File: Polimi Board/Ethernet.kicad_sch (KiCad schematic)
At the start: 17 parts, among them J6 RJ45_Wuerth_7499010121A, U3 LAN8742A

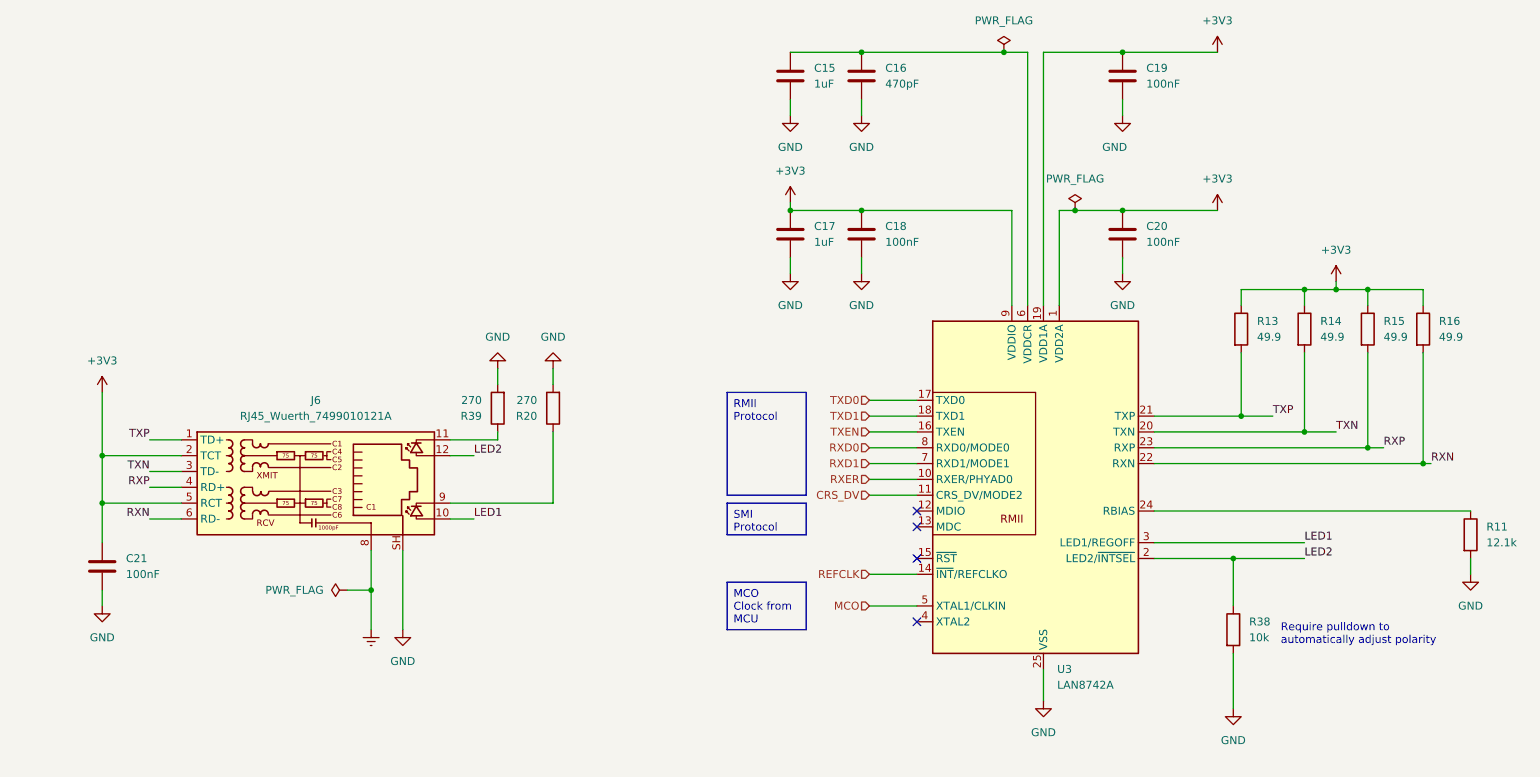
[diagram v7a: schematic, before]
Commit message: adjusted some violations of ERC test
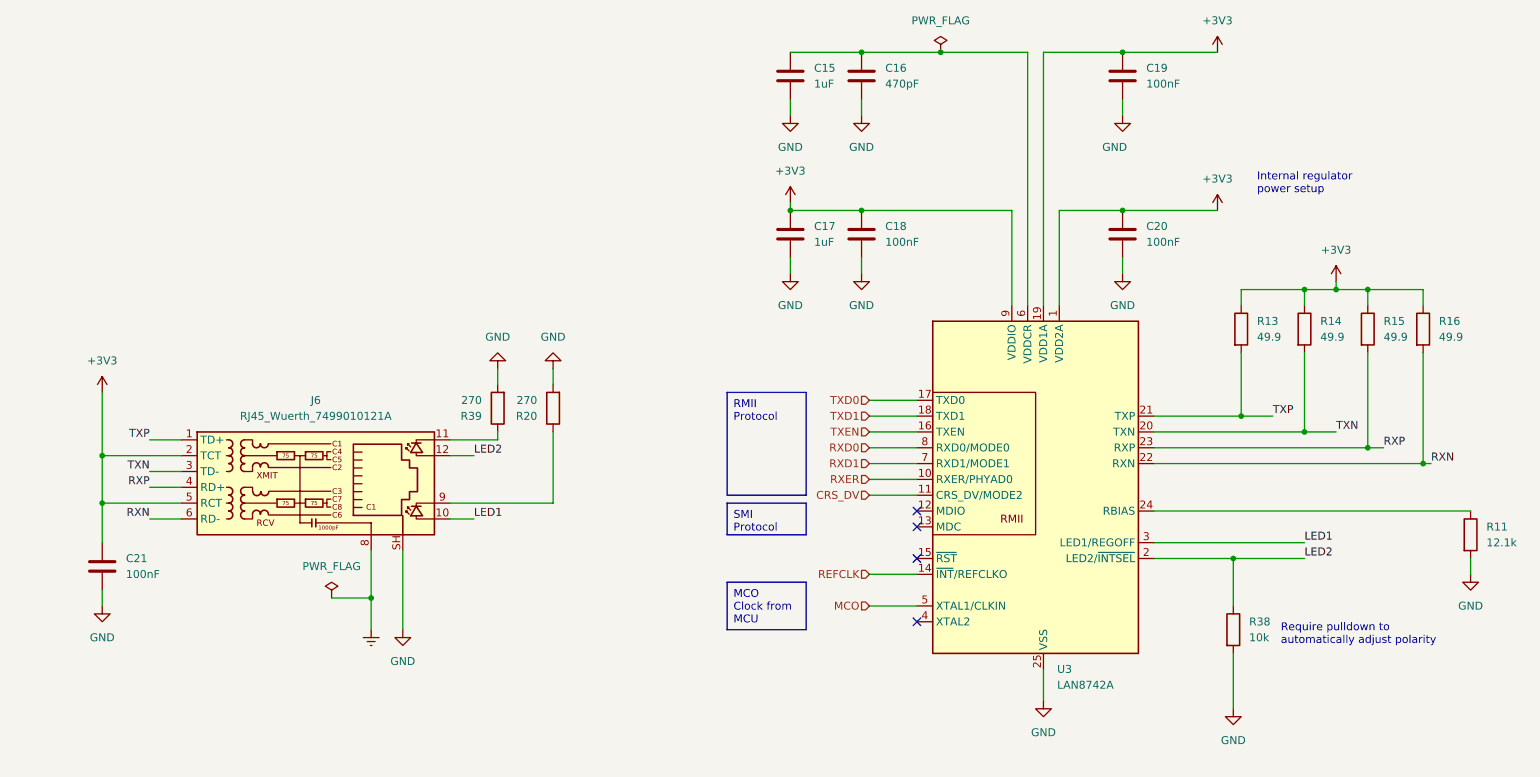
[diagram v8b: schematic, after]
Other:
- note added: "Internal regulator power setup"
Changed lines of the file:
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@@
     (comment 2 "ing. Zaccaria Eliseo Carrettoni")
   )
-  (junction (at 182.88 34.29) (diameter 0) (color 0 0 0 0)
-  )
   (junction (at 236.22 72.39) (diameter 0) (color 0 0 0 0)
   )
@@
   (junction (at 148.59 59.69) (diameter 0) (color 0 0 0 0)
   )
-  (junction (at 194.31 59.69) (diameter 0) (color 0 0 0 0)
-  )
-  (junction (at 81.28 120.65) (diameter 0) (color 0 0 0 0)
-  )
   (junction (at 38.1 106.68) (diameter 0) (color 0 0 0 0)
   )
@@
   (junction (at 160.02 34.29) (diameter 0) (color 0 0 0 0)
   )
+  (junction (at 81.28 121.92) (diameter 0) (color 0 0 0 0)
+  )
   (junction (at 241.3 97.79) (diameter 0) (color 0 0 0 0)
   )
@@
   )
   (junction (at 241.3 72.39) (diameter 0) (color 0 0 0 0)
+  )
+  (junction (at 172.72 34.29) (diameter 0) (color 0 0 0 0)
   )
   (junction (at 160.02 59.69) (diameter 0) (color 0 0 0 0)
@@
     (stroke (width 0) (type default))
   )
-  (wire (pts (xy 160.02 34.29) (xy 182.88 34.29))
-    (stroke (width 0) (type default))
-  )
   (wire (pts (xy 148.59 41.91) (xy 148.59 44.45))
     (stroke (width 0) (type default))
@@
     (stroke (width 0) (type default))
   )
+  (wire (pts (xy 74.93 121.92) (xy 81.28 121.92))
+    (stroke (width 0) (type default))
+  )
   (wire (pts (xy 219.71 130.81) (xy 219.71 139.7))
     (stroke (width 0) (type default))
@@
     (stroke (width 0) (type default))
   )
+  (wire (pts (xy 81.28 121.92) (xy 81.28 127))
+    (stroke (width 0) (type default))
+  )
+  (wire (pts (xy 81.28 114.3) (xy 81.28 121.92))
+    (stroke (width 0) (type default))
+  )
   (wire (pts (xy 161.29 105.41) (xy 168.91 105.41))
     (stroke (width 0) (type default))
@@
     (stroke (width 0) (type default))
   )
-  (wire (pts (xy 201.93 59.69) (xy 194.31 59.69))
-    (stroke (width 0) (type default))
-  )
   (wire (pts (xy 45.72 109.22) (xy 50.8 109.22))
     (stroke (width 0) (type default))
@@
     (stroke (width 0) (type default))
   )
-  (wire (pts (xy 81.28 120.65) (xy 81.28 127))
-    (stroke (width 0) (type default))
-  )
   (wire (pts (xy 250.19 72.39) (xy 250.19 74.93))
     (stroke (width 0) (type default))
@@
     (stroke (width 0) (type default))
   )
-  (wire (pts (xy 81.28 114.3) (xy 81.28 120.65))
-    (stroke (width 0) (type default))
-  )
   (wire (pts (xy 110.49 106.68) (xy 110.49 95.25))
     (stroke (width 0) (type default))
@@
     (stroke (width 0) (type default))
   )
-  (wire (pts (xy 182.88 34.29) (xy 186.69 34.29))
+  (wire (pts (xy 160.02 34.29) (xy 172.72 34.29))
     (stroke (width 0) (type default))
   )
@@
     (stroke (width 0) (type default))
   )
-  (wire (pts (xy 194.31 59.69) (xy 191.77 59.69))
+  (wire (pts (xy 191.77 59.69) (xy 201.93 59.69))
     (stroke (width 0) (type default))
   )
@@
     (stroke (width 0) (type default))
   )
+  (wire (pts (xy 172.72 34.29) (xy 186.69 34.29))
+    (stroke (width 0) (type default))
+  )
   (wire (pts (xy 231.14 82.55) (xy 231.14 95.25))
     (stroke (width 0) (type default))
@@
   )
   (wire (pts (xy 207.01 95.25) (xy 231.14 95.25))
-    (stroke (width 0) (type default))
-  )
-  (wire (pts (xy 77.47 120.65) (xy 81.28 120.65))
     (stroke (width 0) (type default))
   )
@@
     (fill (type none))
     (effects (font (size 1.27 1.27)) (justify left top))
+  )
+  (text "Internal regulator \npower setup" (at 223.52 57.15 0)
+    (effects (font (size 1.27 1.27)) (justify left bottom))
   )
   (text "Require pulldown to \nautomatically adjust polarity"
@@
     (effects (font (size 1.27 1.27)) (justify right))
   )
-  (symbol (lib_id "power:PWR_FLAG") (at 77.47 120.65 90) (unit 1)
-    (in_bom yes) (on_board yes) (dnp no) (fields_autoplaced)
-    (property "Reference" "#FLG06" (at 75.565 120.65 0)
-      (effects (font (size 1.27 1.27)) hide)
-    )
-    (property "Value" "PWR_FLAG" (at 73.66 120.65 90)
-      (effects (font (size 1.27 1.27)) (justify left))
-    )
-    (property "Footprint" "" (at 77.47 120.65 0)
-      (effects (font (size 1.27 1.27)) hide)
-    )
-    (property "Datasheet" "~" (at 77.47 120.65 0)
-      (effects (font (size 1.27 1.27)) hide)
-    )
-    (pin "1")
-    (instances
-      (project "Polimi Board"
-        (path "/319fe76e-1f98-44b3-99b0-af1a9ad7322c/2985c2dc-97fe-4379-8500-18b000a93b2c"
-          (reference "#FLG06") (unit 1)
-        )
-      )
-    )
-  )
   (symbol (lib_id "power:+3V3") (at 38.1 88.9 0) (unit 1)
     (in_bom yes) (on_board yes) (dnp no) (fields_autoplaced)
@@
     )
   )
-  (symbol (lib_id "power:PWR_FLAG") (at 182.88 34.29 0) (unit 1)
-    (in_bom yes) (on_board yes) (dnp no) (fields_autoplaced)
-    (property "Reference" "#FLG04" (at 182.88 32.385 0)
-      (effects (font (size 1.27 1.27)) hide)
-    )
-    (property "Value" "PWR_FLAG" (at 182.88 29.21 0)
-      (effects (font (size 1.27 1.27)))
-    )
-    (property "Footprint" "" (at 182.88 34.29 0)
-      (effects (font (size 1.27 1.27)) hide)
-    )
-    (property "Datasheet" "~" (at 182.88 34.29 0)
-      (effects (font (size 1.27 1.27)) hide)
-    )
-    (pin "1")
-    (instances
-      (project "Polimi Board"
-        (path "/319fe76e-1f98-44b3-99b0-af1a9ad7322c/2985c2dc-97fe-4379-8500-18b000a93b2c"
-          (reference "#FLG04") (unit 1)
-        )
-      )
-    )
-  )
   (symbol (lib_id "power:GND") (at 148.59 69.85 0) (unit 1)
     (in_bom yes) (on_board yes) (dnp no) (fields_autoplaced)
@@
         (path "/319fe76e-1f98-44b3-99b0-af1a9ad7322c/2985c2dc-97fe-4379-8500-18b000a93b2c"
           (reference "#PWR038") (unit 1)
+        )
+      )
+    )
+  )
+  (symbol (lib_id "power:PWR_FLAG") (at 172.72 34.29 0) (unit 1)
+    (in_bom yes) (on_board yes) (dnp no) (fields_autoplaced)
+    (property "Reference" "#FLG01" (at 172.72 32.385 0)
+      (effects (font (size 1.27 1.27)) hide)
+    )
+    (property "Value" "PWR_FLAG" (at 172.72 29.21 0)
+      (effects (font (size 1.27 1.27)))
+    )
+    (property "Footprint" "" (at 172.72 34.29 0)
+      (effects (font (size 1.27 1.27)) hide)
+    )
+    (property "Datasheet" "~" (at 172.72 34.29 0)
+      (effects (font (size 1.27 1.27)) hide)
+    )
+    (pin "1")
+    (instances
+      (project "Polimi Board"
+        (path "/319fe76e-1f98-44b3-99b0-af1a9ad7322c/2985c2dc-97fe-4379-8500-18b000a93b2c"
+          (reference "#FLG01") (unit 1)
         )
       )
@@
     )
   )
+  (symbol (lib_id "power:PWR_FLAG") (at 74.93 121.92 0) (unit 1)
+    (in_bom yes) (on_board yes) (dnp no) (fields_autoplaced)
+    (property "Reference" "#FLG03" (at 74.93 120.015 0)
+      (effects (font (size 1.27 1.27)) hide)
+    )
+    (property "Value" "PWR_FLAG" (at 74.93 116.84 0)
+      (effects (font (size 1.27 1.27)))
+    )
+    (property "Footprint" "" (at 74.93 121.92 0)
+      (effects (font (size 1.27 1.27)) hide)
+    )
+    (property "Datasheet" "~" (at 74.93 121.92 0)
+      (effects (font (size 1.27 1.27)) hide)
+    )
+    (pin "1")
+    (instances
+      (project "Polimi Board"
+        (path "/319fe76e-1f98-44b3-99b0-af1a9ad7322c/2985c2dc-97fe-4379-8500-18b000a93b2c"
+          (reference "#FLG03") (unit 1)
+        )
+      )
+    )
+  )
   (symbol (lib_id "Device:C") (at 148.59 38.1 0) (unit 1)
     (in_bom yes) (on_board yes) (dnp no) (fields_autoplaced)
@@
         )
       )
-    )
-  )
-  (symbol (lib_id "power:PWR_FLAG") (at 194.31 59.69 0) (unit 1)
-    (in_bom yes) (on_board yes) (dnp no) (fields_autoplaced)
-    (property "Reference" "#FLG03" (at 194.31 57.785 0)
-      (effects (font (size 1.27 1.27)) hide)
-    )
-    (property "Value" "PWR_FLAG" (at 194.31 54.61 0)
-      (effects (font (size 1.27 1.27)))
-    )
-    (property "Footprint" "" (at 194.31 59.69 0)
-      (effects (font (size 1.27 1.27)) hide)
-    )
-    (property "Datasheet" "~" (at 194.31 59.69 0)
-      (effects (font (size 1.27 1.27)) hide)
-    )
-    (pin "1")
-    (instances
-      (project "Polimi Board"
-        (path "/319fe76e-1f98-44b3-99b0-af1a9ad7322c/2985c2dc-97fe-4379-8500-18b000a93b2c"
-          (reference "#FLG03") (unit 1)
-        )
-      )
